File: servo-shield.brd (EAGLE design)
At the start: 65 x 56 mm, 7 parts, among them IC1 24AA01P, K1 PIN20X2

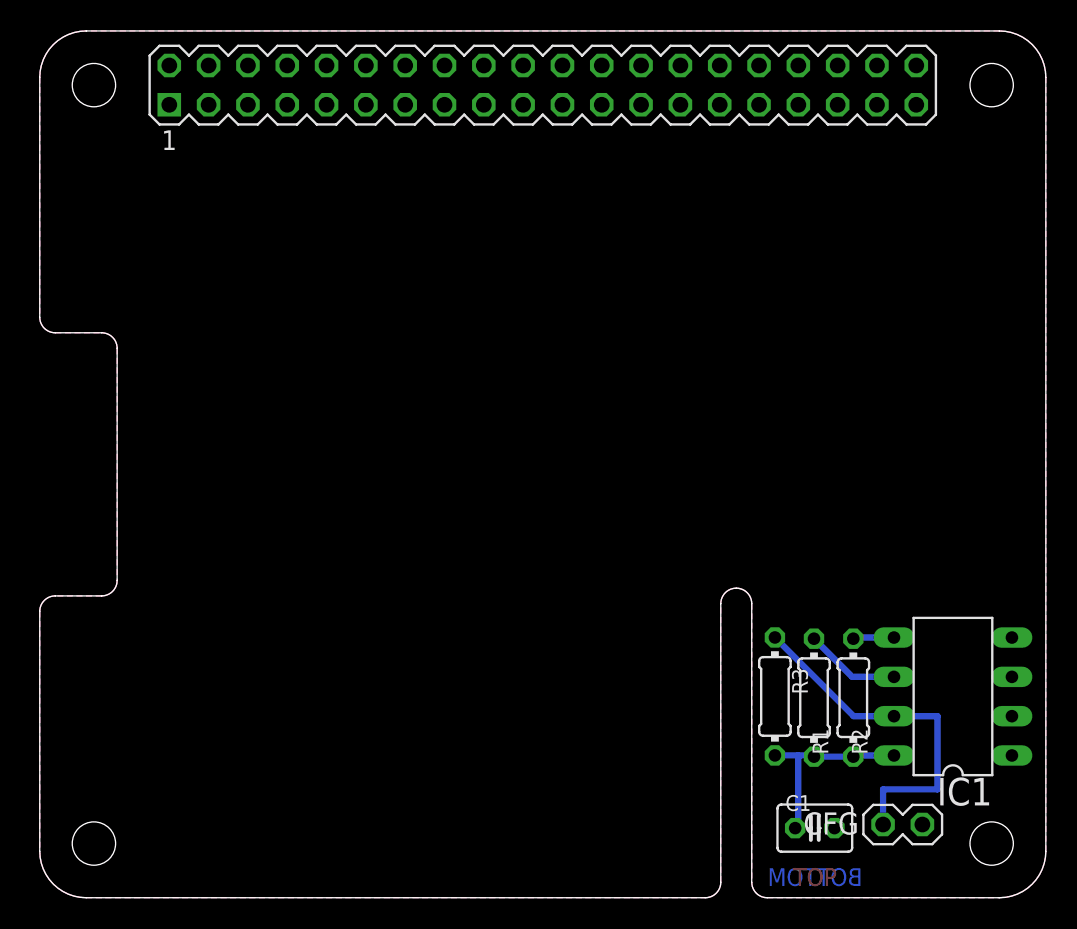
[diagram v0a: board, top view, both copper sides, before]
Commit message: Add PCA9685
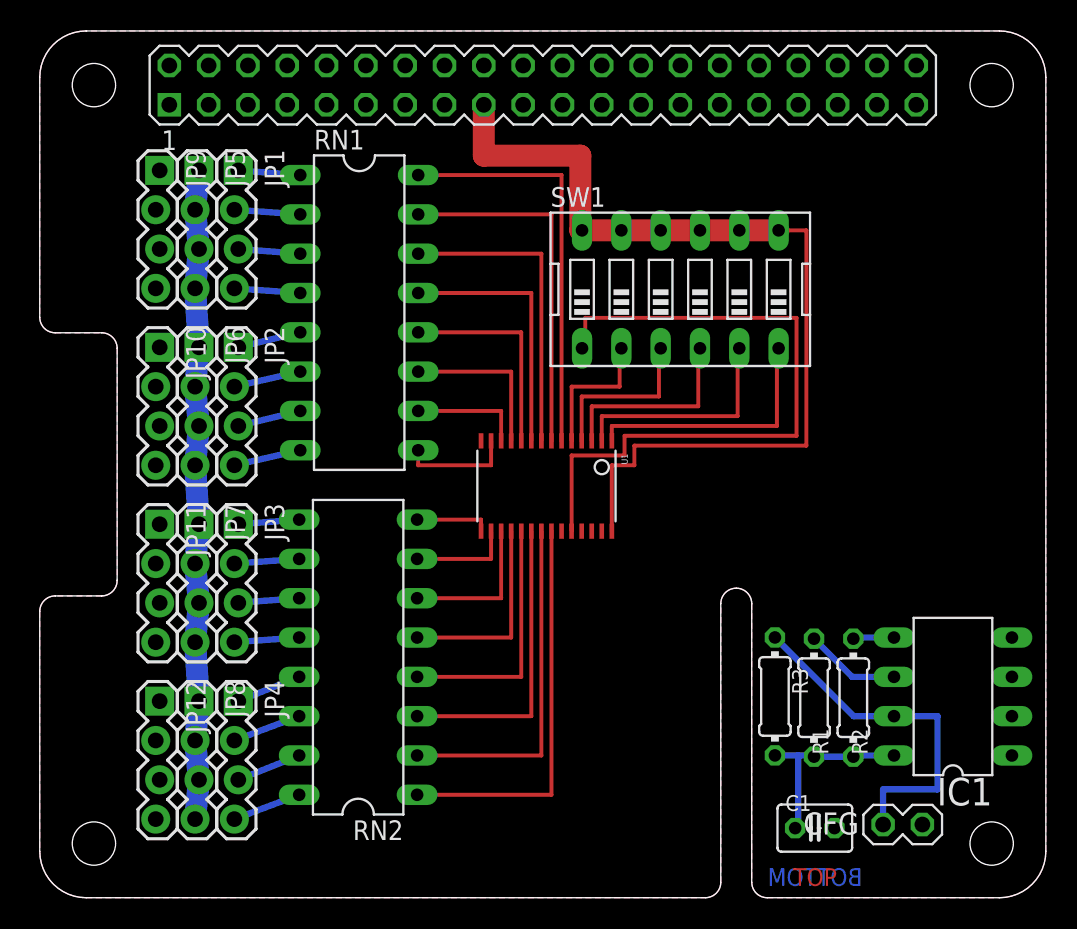
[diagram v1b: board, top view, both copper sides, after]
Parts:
- added JP1, JP10, JP11, JP12, JP2, JP3, JP4, JP5, JP6, JP7, JP8, JP9: (no value), SparkFun-Connectors:1X04_LOCK
- added RN1, RN2: (no value), resistor-dil:DIL16
- added SW1: (no value), special:EDG-06
- added U1: (no value), adafruit:TSSOP28
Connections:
- new net I2C_SCL: U1.26
- new net I2C_SDA: U1.27
- new net N$1: RN2.7, U1.16
- new net N$10: JP3.2, RN2.10
- new net N$11: SW1.1, U1.24
- new net N$12: SW1.2, U1.5
- new net N$13: SW1.3, U1.4
- new net N$14: SW1.4, U1.3
- new net N$15: SW1.5, U1.2
- new net N$16: SW1.6, U1.1
- new net N$17: JP3.3, RN2.11
- new net N$18: JP3.4, RN2.12
- new net N$19: JP4.1, RN2.13
- new net N$2: RN2.8, U1.15
- new net N$20: JP4.2, RN2.14
- new net N$21: JP4.3, RN2.15
- new net N$22: JP4.4, RN2.16
- new net N$23: RN2.1, U1.22
- new net N$24: RN2.2, U1.21
- new net N$25: RN2.3, U1.20
- new net N$26: RN2.4, U1.19
- new net N$27: RN2.5, U1.18
- new net N$28: RN2.6, U1.17
- new net N$29: RN1.10, U1.12
- new net N$3: RN1.9, U1.13
- new net N$30: RN1.11, U1.11
- new net N$31: RN1.12, U1.10
- new net N$32: RN1.13, U1.9
- new net N$33: RN1.14, U1.8
- new net N$34: RN1.15, U1.7
- new net N$35: RN1.16, U1.6
- new net N$36: JP2.1, RN1.5
- new net N$37: JP2.4, RN1.8
- new net N$38: JP2.3, RN1.7
- new net N$39: JP2.2, RN1.6
- new net N$5: JP1.4, RN1.4
- new net N$6: JP1.3, RN1.3
- new net N$7: JP1.2, RN1.2
- new net N$8: JP1.1, RN1.1
- new net N$9: JP3.1, RN2.9
- new net V+: JP5.1, JP5.2, JP5.3, JP5.4, JP6.1, JP6.2, JP6.3, JP6.4, JP7.1, JP7.2, JP7.3, JP7.4, JP8.1, JP8.2, JP8.3, JP8.4
- net +3V3: now also SW1.10, SW1.11, SW1.12, SW1.7, SW1.8, SW1.9, U1.28
- net GND: now also JP10.1, JP10.2, JP10.3, JP10.4, JP11.1, JP11.2, JP11.3, JP11.4, JP12.1, JP12.2, JP12.3, JP12.4, JP9.1, JP9.2, JP9.3, JP9.4, U1.14, U1.25
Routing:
- net +3V3: track 12.7 -> 73.7 mm
- net N$11: track 0.00 -> 44.1 mm
- net V+: track 0.00 -> 42.1 mm
- net N$35: track 0.00 -> 26.4 mm
- net N$23: track 0.00 -> 25.7 mm
- net N$34: track 0.00 -> 23.2 mm
- net N$24: track 0.00 -> 22.5 mm
- net N$33: track 0.00 -> 20.1 mm
- net N$25: track 0.00 -> 19.3 mm
- net N$32: track 0.00 -> 16.9 mm
- net N$16: track 0.00 -> 16.8 mm
- net N$26: track 0.00 -> 16.1 mm
- net N$15: track 0.00 -> 14.9 mm
- net N$31: track 0.00 -> 13.7 mm
- net N$14: track 0.00 -> 13.0 mm
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
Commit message: Finished current schematic.. Must add power supply and power regulation
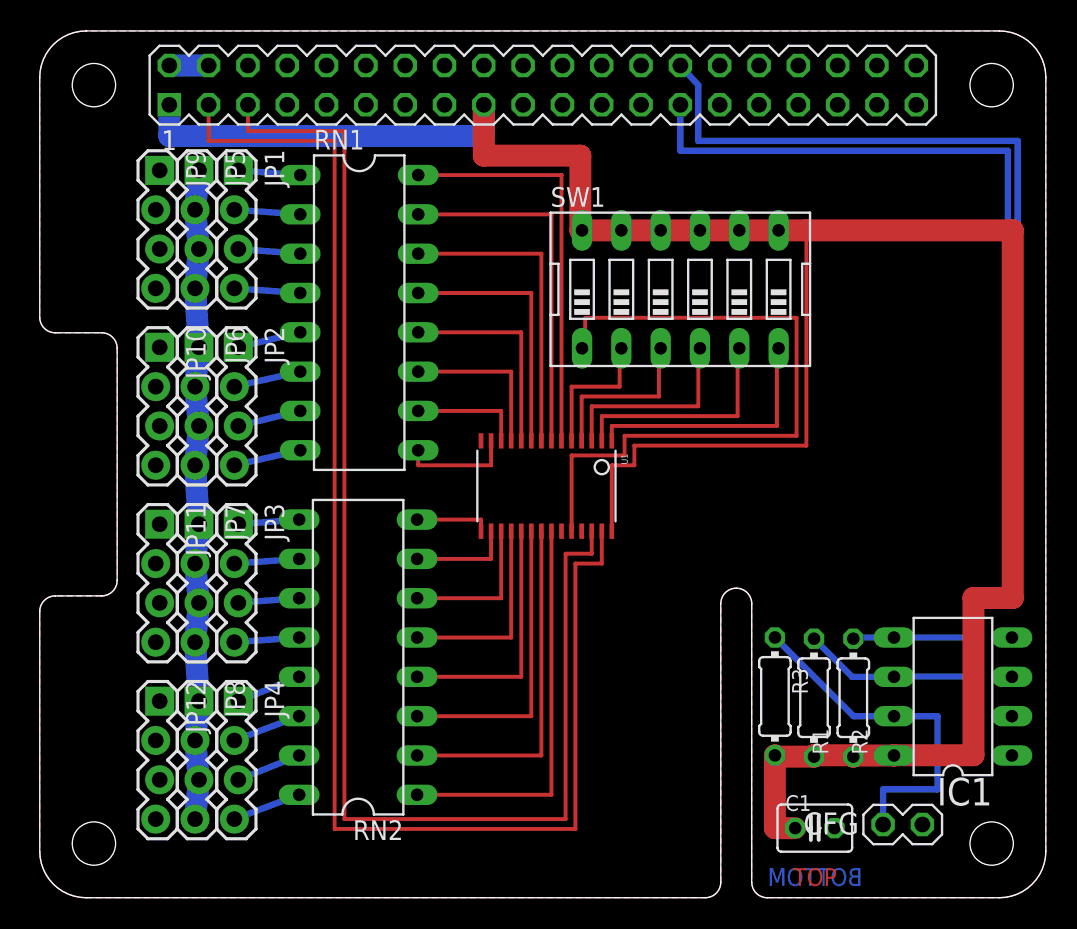
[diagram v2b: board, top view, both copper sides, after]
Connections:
- net I2C_SCL: now also K1.5
- net I2C_SDA: now also K1.3
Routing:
- net I2C_SDA: track 0.00 -> 91.4 mm
- net I2C_SCL: track 0.00 -> 87.0 mm
- net +3V3: track 73.7 -> 154.3 mm
- net ID_SCL: track 6.19 -> 74.8 mm
- net ID_SDA: track 2.66 -> 65.6 mm
- net +5V: track 0.00 -> 2.54 mm
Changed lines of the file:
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@@
 <contactref element="R2" pad="2"/>
 <contactref element="R1" pad="2"/>
-<wire x1="47.4975" y1="9.195" x2="49" y2="9.195" width="0.4064" layer="16"/>
-<wire x1="49" y1="9.195" x2="50.0225" y2="9.195" width="0.4064" layer="16"/>
-<wire x1="50.0225" y1="9.195" x2="50.0225" y2="9.115" width="0.4064" layer="16"/>
-<wire x1="52.5625" y1="9.115" x2="50.0225" y2="9.115" width="0.4064" layer="16"/>
-<wire x1="55.19" y1="9.19" x2="52.5625" y2="9.19" width="0.4064" layer="16"/>
-<wire x1="52.5625" y1="9.19" x2="52.5625" y2="9.115" width="0.4064" layer="16"/>
-<wire x1="48.805" y1="4.4975" x2="49" y2="4.4975" width="0.4064" layer="16"/>
-<wire x1="49" y1="4.4975" x2="49" y2="9.195" width="0.4064" layer="16"/>
 <contactref element="U1" pad="28"/>
 <contactref element="SW1" pad="12"/>
@@
 <wire x1="38.4175" y1="29.21" x2="49.53" y2="29.21" width="0.254" layer="1"/>
 <wire x1="49.53" y1="29.21" x2="49.53" y2="43.1175" width="0.254" layer="1"/>
-<wire x1="49.53" y1="43.1175" x2="47.735" y2="43.1175" width="0.254" layer="1"/>
-<wire x1="28.69" y1="51.23" x2="8.37" y2="51.23" width="0" layer="19" extent="1-1"/>
-<wire x1="47.4975" y1="9.195" x2="36.96" y2="23.6822" width="0" layer="19" extent="1-1"/>
+<wire x1="60.325" y1="9.2075" x2="60.325" y2="19.3675" width="1.4224" layer="1"/>
+<wire x1="60.325" y1="19.3675" x2="62.865" y2="19.3675" width="1.4224" layer="1"/>
+<wire x1="62.865" y1="19.3675" x2="62.865" y2="43.1175" width="1.4224" layer="1"/>
+<wire x1="49.53" y1="43.1175" x2="62.865" y2="43.1175" width="1.4224" layer="1"/>
+<wire x1="49.53" y1="43.1175" x2="47.735" y2="43.1175" width="1.4224" layer="1"/>
+<wire x1="52.5625" y1="9.2075" x2="52.5625" y2="9.115" width="1.4224" layer="1"/>
+<wire x1="52.5625" y1="9.2075" x2="50.0225" y2="9.2075" width="1.4224" layer="1"/>
+<wire x1="50.0225" y1="9.2075" x2="50.0225" y2="9.115" width="1.4224" layer="1"/>
+<wire x1="50.0225" y1="9.115" x2="47.4975" y2="9.115" width="1.4224" layer="1"/>
+<wire x1="47.4975" y1="9.115" x2="47.4975" y2="9.195" width="1.4224" layer="1"/>
+<wire x1="48.805" y1="4.4975" x2="47.4975" y2="4.4975" width="1.4224" layer="1"/>
+<wire x1="47.4975" y1="4.4975" x2="47.4975" y2="9.195" width="1.4224" layer="1"/>
+<wire x1="28.69" y1="51.23" x2="28.69" y2="49.2125" width="1.4224" layer="16"/>
+<wire x1="28.69" y1="49.2125" x2="8.37" y2="49.2125" width="1.4224" layer="16"/>
+<wire x1="8.37" y1="51.23" x2="8.37" y2="49.2125" width="1.4224" layer="16"/>
+<wire x1="52.5625" y1="9.115" x2="52.5625" y2="9.19" width="1.4224" layer="1"/>
+<wire x1="52.5625" y1="9.19" x2="55.19" y2="9.19" width="1.4224" layer="1"/>
+<wire x1="55.19" y1="9.19" x2="55.19" y2="9.2075" width="1.4224" layer="1"/>
+<wire x1="55.19" y1="9.2075" x2="60.325" y2="9.2075" width="1.4224" layer="1"/>
 </signal>
 <signal name="+5V">
 <contactref element="K1" pad="2"/>
 <contactref element="K1" pad="4"/>
-<wire x1="8.37" y1="53.77" x2="10.91" y2="53.77" width="0" layer="19" extent="1-1"/>
+<wire x1="8.37" y1="53.77" x2="10.91" y2="53.77" width="1.4224" layer="16"/>
 </signal>
 <signal name="N$4">
@@
 <wire x1="55.19" y1="14.27" x2="52.4875" y2="14.27" width="0.4064" layer="16"/>
 <wire x1="52.4875" y1="14.27" x2="50.0225" y2="16.735" width="0.4064" layer="16"/>
-<wire x1="50.0225" y1="16.735" x2="41.39" y2="53.77" width="0" layer="19" extent="1-1"/>
+<wire x1="41.39" y1="53.77" x2="42.545" y2="52.5" width="0.4064" layer="16"/>
+<wire x1="42.545" y1="52.5" x2="42.545" y2="48.895" width="0.4064" layer="16"/>
+<wire x1="42.545" y1="48.895" x2="63.1825" y2="48.895" width="0.4064" layer="16"/>
+<wire x1="63.1825" y1="48.895" x2="63.1825" y2="19.05" width="0.4064" layer="16"/>
+<wire x1="63.1825" y1="19.05" x2="60.6425" y2="19.05" width="0.4064" layer="16"/>
+<wire x1="60.6425" y1="19.05" x2="60.6425" y2="14.2875" width="0.4064" layer="16"/>
+<wire x1="60.6425" y1="14.2875" x2="55.19" y2="14.2875" width="0.4064" layer="16"/>
+<wire x1="55.19" y1="14.2875" x2="55.19" y2="14.27" width="0.4064" layer="16"/>
 </signal>
 <signal name="ID_SDA">
@@
 <wire x1="55.19" y1="16.81" x2="52.6375" y2="16.81" width="0.4064" layer="16"/>
 <wire x1="52.6375" y1="16.81" x2="52.5625" y2="16.735" width="0.4064" layer="16"/>
-<wire x1="52.6375" y1="16.81" x2="41.39" y2="51.23" width="0" layer="19" extent="16-16"/>
+<wire x1="41.39" y1="51.23" x2="41.39" y2="48.26" width="0.4064" layer="16"/>
+<wire x1="41.39" y1="48.26" x2="62.5475" y2="48.26" width="0.4064" layer="16"/>
+<wire x1="62.5475" y1="48.26" x2="62.5475" y2="19.685" width="0.4064" layer="16"/>
+<wire x1="62.5475" y1="19.685" x2="60.0075" y2="19.685" width="0.4064" layer="16"/>
+<wire x1="60.0075" y1="19.685" x2="60.0075" y2="16.81" width="0.4064" layer="16"/>
+<wire x1="60.0075" y1="16.81" x2="55.19" y2="16.81" width="0.4064" layer="16"/>
 </signal>
 <signal name="N$11">
@@
 <signal name="I2C_SDA">
 <contactref element="U1" pad="27"/>
+<contactref element="K1" pad="3"/>
+<wire x1="10.91" y1="51.23" x2="10.91" y2="48.895" width="0.254" layer="1"/>
+<wire x1="10.91" y1="48.895" x2="19.05" y2="48.895" width="0.254" layer="1"/>
+<wire x1="19.05" y1="48.895" x2="19.05" y2="4.445" width="0.254" layer="1"/>
+<wire x1="19.05" y1="4.445" x2="34.6075" y2="4.445" width="0.254" layer="1"/>
+<wire x1="34.6075" y1="4.445" x2="34.6075" y2="21.59" width="0.254" layer="1"/>
+<wire x1="34.6075" y1="21.59" x2="36.31" y2="21.59" width="0.254" layer="1"/>
+<wire x1="36.31" y1="23.6822" x2="36.31" y2="21.59" width="0.254" layer="1"/>
 </signal>
 <signal name="I2C_SCL">
 <contactref element="U1" pad="26"/>
+<contactref element="K1" pad="5"/>
+<wire x1="35.66" y1="23.6822" x2="35.66" y2="22.225" width="0.254" layer="1"/>
+<wire x1="35.66" y1="22.225" x2="33.9725" y2="22.225" width="0.254" layer="1"/>
+<wire x1="33.9725" y1="22.225" x2="33.9725" y2="5.08" width="0.254" layer="1"/>
+<wire x1="33.9725" y1="5.08" x2="19.685" y2="5.08" width="0.254" layer="1"/>
+<wire x1="19.685" y1="5.08" x2="19.685" y2="49.53" width="0.254" layer="1"/>
+<wire x1="19.685" y1="49.53" x2="13.45" y2="49.53" width="0.254" layer="1"/>
+<wire x1="13.45" y1="51.23" x2="13.45" y2="49.53" width="0.254" layer="1"/>
 </signal>
 <signal name="N$5">
